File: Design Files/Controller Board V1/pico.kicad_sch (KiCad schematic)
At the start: 0 parts

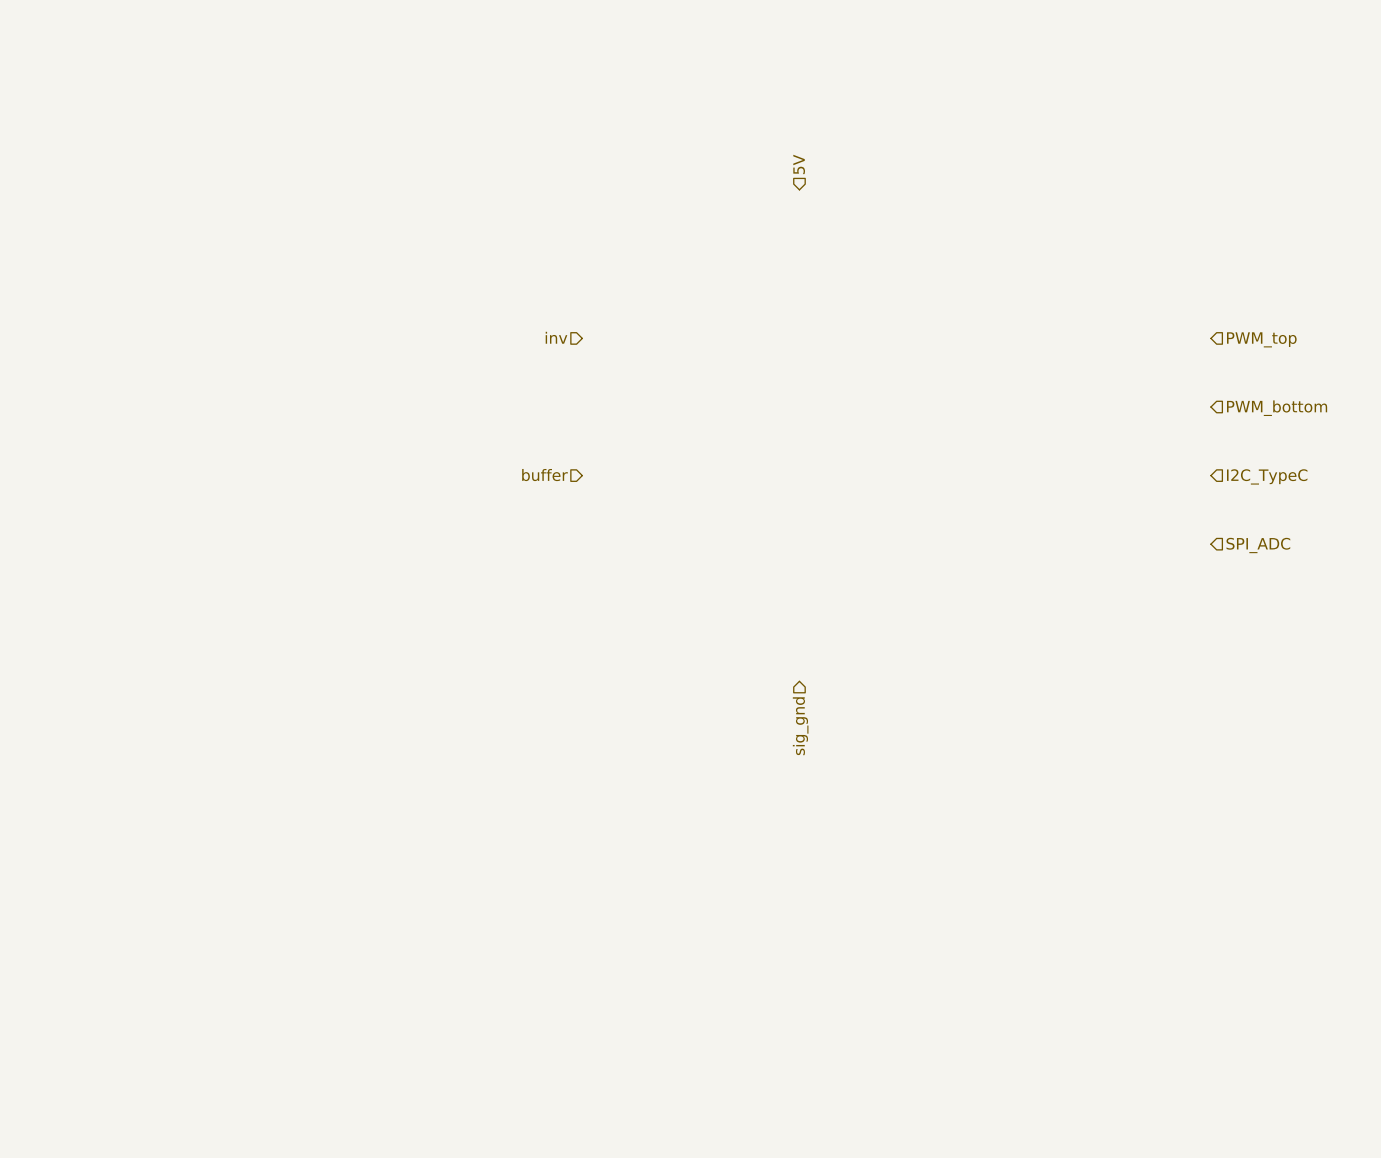
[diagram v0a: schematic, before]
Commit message: Pico Schematic Started
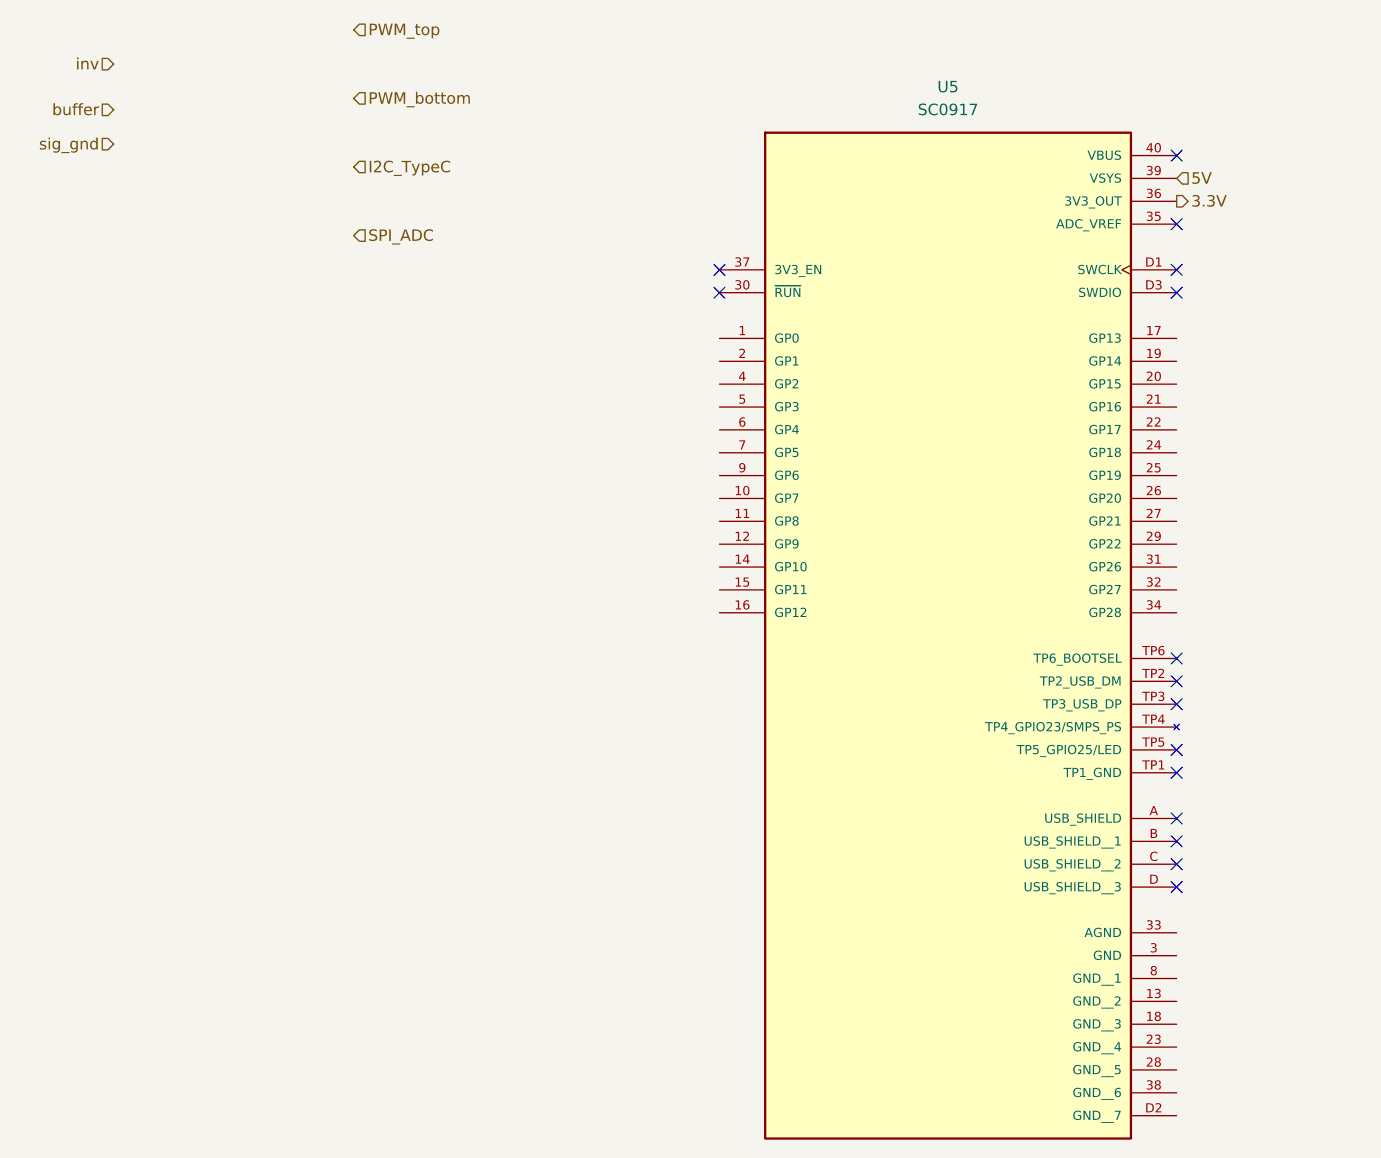
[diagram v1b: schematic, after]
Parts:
- added U5: SC0917, SC0917:MODULE_SC0917, symbol PassiveBankV1:SC0917
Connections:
- net 5V: now also U5.39 (VSYS)
- new net 3.3V: U5.36 (3V3_OUT)
- no-connect marks 0 -> 15

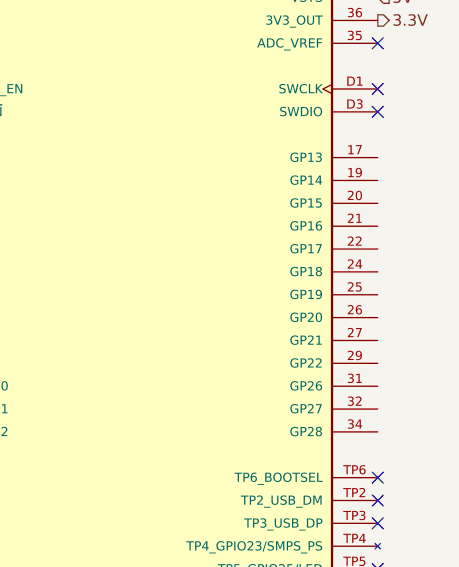
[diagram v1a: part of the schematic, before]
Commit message: I2C channels for pico and current sensors
gaming B)
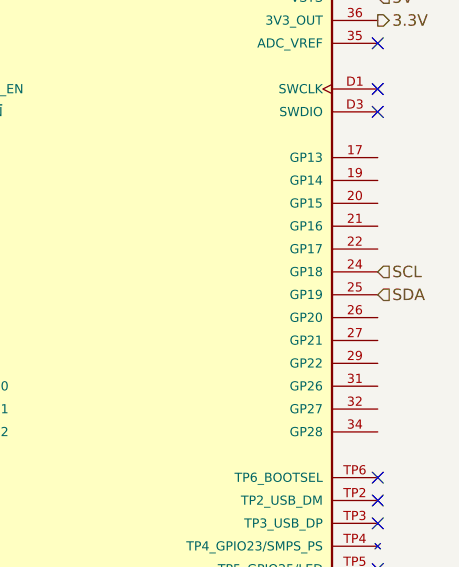
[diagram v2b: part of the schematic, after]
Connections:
- net SCL: now reaches U5.24 (GP18)
- net SDA: now reaches U5.25 (GP19)
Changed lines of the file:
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@@
 		(shape input)
 		(at 67.31 41.91 0)
+		(fields_autoplaced yes)
 		(effects
 			(font
@@
 		(shape input)
 		(at 40.64 46.99 180)
+		(fields_autoplaced yes)
 		(effects
 			(font
@@
 		(shape input)
 		(at 40.64 38.1 180)
+		(fields_autoplaced yes)
 		(effects
 			(font
@@
 		(shape output)
 		(at 158.75 53.34 0)
+		(fields_autoplaced yes)
 		(effects
 			(font
@@
 		(shape input)
 		(at 67.31 49.53 0)
+		(fields_autoplaced yes)
+		(effects
+			(font
+				(size 1.27 1.27)
+			)
+			(justify left)
+		)
+	)
+	(hierarchical_label "SCL"
+		(shape input)
+		(at 158.75 81.28 0)
+		(fields_autoplaced yes)
 		(effects
 			(font
@@
 		(shape input)
 		(at 67.31 57.15 0)
+		(fields_autoplaced yes)
+		(effects
+			(font
+				(size 1.27 1.27)
+			)
+			(justify left)
+		)
+	)
+	(hierarchical_label "SDA"
+		(shape input)
+		(at 158.75 83.82 0)
+		(fields_autoplaced yes)
 		(effects
 			(font
@@
 		(shape input)
 		(at 158.75 50.8 0)
+		(fields_autoplaced yes)
 		(effects
 			(font
@@
 		(shape input)
 		(at 67.31 34.29 0)
+		(fields_autoplaced yes)
 		(effects
 			(font
@@
 		(shape input)
 		(at 40.64 43.18 180)
+		(fields_autoplaced yes)
 		(effects
 			(font

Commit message: Assigning footprints and ading to schematic
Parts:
- U5: footprint SC0917:MODULE_SC0917 -> Module:RaspberryPi_Pico_Common_THT
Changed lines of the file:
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@@
 		(shape input)
 		(at 67.31 41.91 0)
-		(fields_autoplaced yes)
 		(effects
 			(font
@@
 		(shape input)
 		(at 40.64 46.99 180)
-		(fields_autoplaced yes)
 		(effects
 			(font
@@
 		(shape input)
 		(at 40.64 38.1 180)
-		(fields_autoplaced yes)
 		(effects
 			(font
@@
 		(shape output)
 		(at 158.75 53.34 0)
-		(fields_autoplaced yes)
 		(effects
 			(font
@@
 		(shape input)
 		(at 67.31 49.53 0)
-		(fields_autoplaced yes)
 		(effects
 			(font
@@
 		(shape input)
 		(at 158.75 81.28 0)
-		(fields_autoplaced yes)
 		(effects
 			(font
@@
 		(shape input)
 		(at 67.31 57.15 0)
-		(fields_autoplaced yes)
 		(effects
 			(font
@@
 		(shape input)
 		(at 158.75 83.82 0)
-		(fields_autoplaced yes)
 		(effects
 			(font
@@
 		(shape input)
 		(at 158.75 50.8 0)
-		(fields_autoplaced yes)
 		(effects
 			(font
@@
 		(shape input)
 		(at 67.31 34.29 0)
-		(fields_autoplaced yes)
 		(effects
 			(font
@@
 		(shape input)
 		(at 40.64 43.18 180)
-		(fields_autoplaced yes)
 		(effects
 			(font
@@
 			)
 		)
-		(property "Footprint" "SC0917:MODULE_SC0917"
+		(property "Footprint" "Module:RaspberryPi_Pico_Common_THT"
 			(at 133.35 88.9 0)
 			(effects

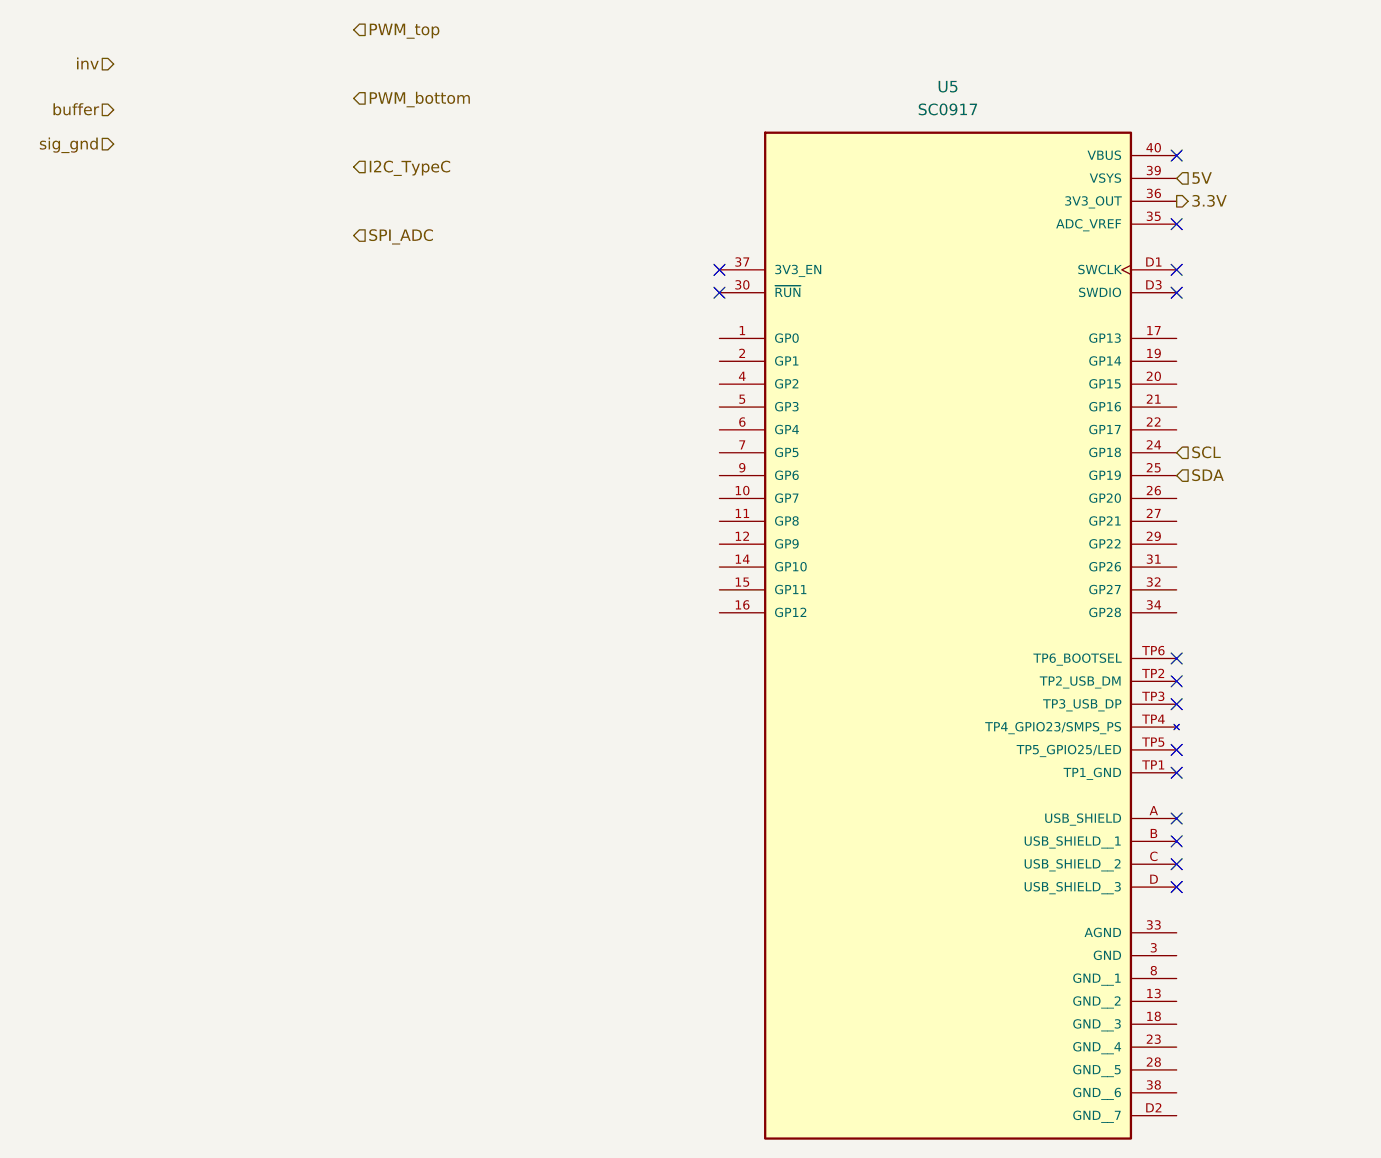
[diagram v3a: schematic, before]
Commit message: Updated pins on PICO schematic
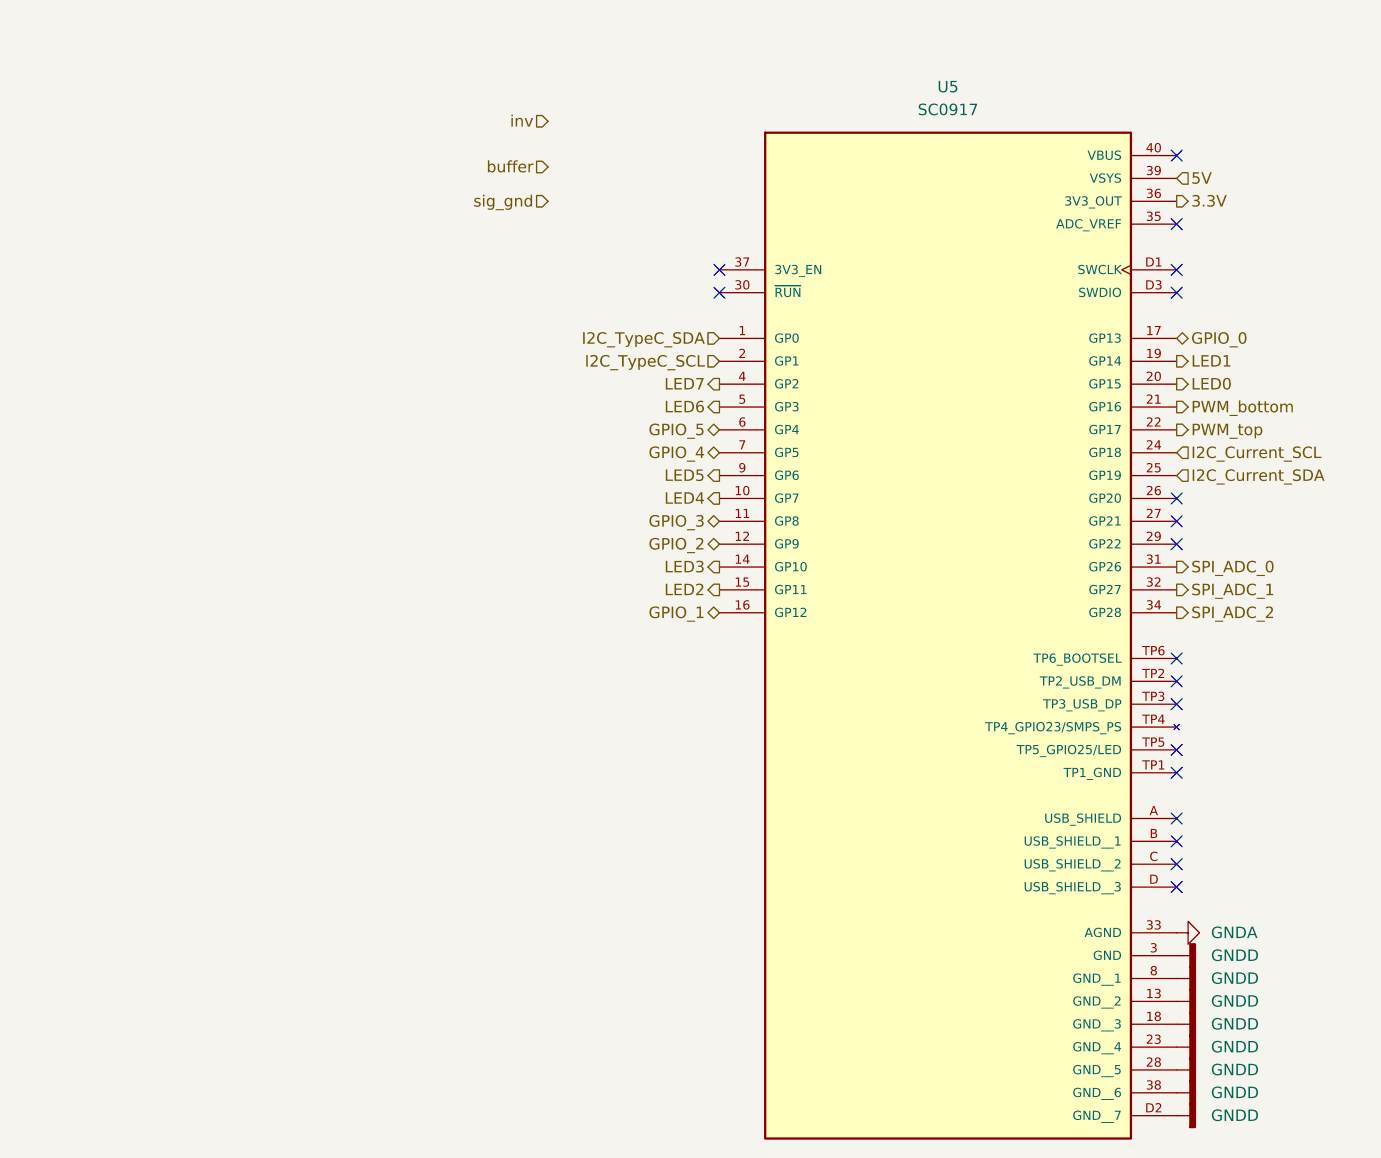
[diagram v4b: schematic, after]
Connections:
- net PWM_bottom: now also U5.21 (GP16)
- net PWM_top: now also U5.22 (GP17)
- net I2C_TypeC_SDA: now reaches U5.1 (GP0)
- net LED4: now reaches U5.10 (GP7)
- net GPIO_3: now reaches U5.11 (GP8)
- net GPIO_2: now reaches U5.12 (GP9)
- net GNDD: now reaches U5.13 (GND__2)
- net GNDD: now also U5.18 (GND__3), U5.23 (GND__4), U5.28 (GND__5), U5.3 (GND), U5.38 (GND__6), U5.8 (GND__1), U5.D2 (GND__7)
- net LED3: now reaches U5.14 (GP10)
- net LED2: now reaches U5.15 (GP11)
- net GPIO_1: now reaches U5.16 (GP12)
- net GPIO_0: now reaches U5.17 (GP13)
- net LED1: now reaches U5.19 (GP14)
- net I2C_TypeC_SCL: now reaches U5.2 (GP1)
- net LED0: now reaches U5.20 (GP15)
- net SPI_ADC_0: now reaches U5.31 (GP26)
- net SPI_ADC_1: now reaches U5.32 (GP27)
- net GNDA: now reaches U5.33 (AGND)
- net SPI_ADC_2: now reaches U5.34 (GP28)
- net LED7: now reaches U5.4 (GP2)
- net LED6: now reaches U5.5 (GP3)
- net GPIO_5: now reaches U5.6 (GP4)
- net GPIO_4: now reaches U5.7 (GP5)
- net LED5: now reaches U5.9 (GP6)
- net SCL renamed I2C_Current_SCL
- net SDA renamed I2C_Current_SDA
- no-connect marks 15 -> 18

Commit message: Major Schematic Progress
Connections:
- net SPI_ADC_0 renamed ADC_0
- net SPI_ADC_1 renamed ADC_1
- net SPI_ADC_2 renamed ADC_2
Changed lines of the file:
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@@
 		(shape bidirectional)
 		(at 107.95 81.28 180)
+		(fields_autoplaced yes)
 		(effects
 			(font
@@
 		(shape bidirectional)
 		(at 107.95 91.44 180)
-		(effects
-			(font
-				(size 1.27 1.27)
-			)
-			(justify right)
-		)
-	)
-	(hierarchical_label "SPI_ADC_1"
+		(fields_autoplaced yes)
+		(effects
+			(font
+				(size 1.27 1.27)
+			)
+			(justify right)
+		)
+	)
+	(hierarchical_label "ADC_1"
 		(shape output)
 		(at 158.75 96.52 0)
+		(fields_autoplaced yes)
 		(effects
 			(font
@@
 		(shape bidirectional)
 		(at 107.95 78.74 180)
+		(fields_autoplaced yes)
 		(effects
 			(font
@@
 		(shape output)
 		(at 158.75 76.2 0)
+		(fields_autoplaced yes)
 		(effects
 			(font
@@
 		(shape input)
 		(at 88.9 53.34 180)
+		(fields_autoplaced yes)
 		(effects
 			(font
@@
 		(shape input)
 		(at 88.9 44.45 180)
+		(fields_autoplaced yes)
 		(effects
 			(font
@@
 		(shape output)
 		(at 107.95 83.82 180)
+		(fields_autoplaced yes)
 		(effects
 			(font
@@
 		(shape output)
 		(at 107.95 73.66 180)
+		(fields_autoplaced yes)
 		(effects
 			(font
@@
 		(shape output)
 		(at 107.95 93.98 180)
+		(fields_autoplaced yes)
 		(effects
 			(font
@@
 		(shape output)
 		(at 158.75 73.66 0)
+		(fields_autoplaced yes)
 		(effects
 			(font
@@
 		(shape output)
 		(at 158.75 53.34 0)
+		(fields_autoplaced yes)
 		(effects
 			(font
@@
 		(shape input)
 		(at 107.95 68.58 180)
+		(fields_autoplaced yes)
 		(effects
 			(font
@@
 		(shape bidirectional)
 		(at 158.75 68.58 0)
+		(fields_autoplaced yes)
 		(effects
 			(font
@@
 	)
 	(hierarchical_label "I2C_Current_SCL"
-		(shape input)
+		(shape bidirectional)
 		(at 158.75 81.28 0)
-		(effects
-			(font
-				(size 1.27 1.27)
-			)
-			(justify left)
-		)
-	)
-	(hierarchical_label "SPI_ADC_0"
+		(fields_autoplaced yes)
+		(effects
+			(font
+				(size 1.27 1.27)
+			)
+			(justify left)
+		)
+	)
+	(hierarchical_label "ADC_0"
 		(shape output)
 		(at 158.75 93.98 0)
+		(fields_autoplaced yes)
 		(effects
 			(font
@@
 		(shape bidirectional)
 		(at 107.95 88.9 180)
+		(fields_autoplaced yes)
 		(effects
 			(font
@@
 		(shape input)
 		(at 107.95 71.12 180)
-		(effects
-			(font
-				(size 1.27 1.27)
-			)
-			(justify right)
-		)
-	)
-	(hierarchical_label "SPI_ADC_2"
+		(fields_autoplaced yes)
+		(effects
+			(font
+				(size 1.27 1.27)
+			)
+			(justify right)
+		)
+	)
+	(hierarchical_label "ADC_2"
 		(shape output)
 		(at 158.75 99.06 0)
+		(fields_autoplaced yes)
 		(effects
 			(font
@@
 		(shape output)
 		(at 107.95 86.36 180)
+		(fields_autoplaced yes)
 		(effects
 			(font
@@
 	)
 	(hierarchical_label "I2C_Current_SDA"
-		(shape input)
+		(shape bidirectional)
 		(at 158.75 83.82 0)
+		(fields_autoplaced yes)
 		(effects
 			(font
@@
 		(shape input)
 		(at 158.75 50.8 0)
+		(fields_autoplaced yes)
 		(effects
 			(font
@@
 		(shape bidirectional)
 		(at 107.95 99.06 180)
+		(fields_autoplaced yes)
 		(effects
 			(font
@@
 		(shape output)
 		(at 107.95 76.2 180)
+		(fields_autoplaced yes)
 		(effects
 			(font
@@
 		(shape output)
 		(at 158.75 78.74 0)
+		(fields_autoplaced yes)
 		(effects
 			(font
@@
 		(shape input)
 		(at 88.9 49.53 180)
+		(fields_autoplaced yes)
 		(effects
 			(font
@@
 		(shape output)
 		(at 158.75 71.12 0)
+		(fields_autoplaced yes)
 		(effects
 			(font
@@
 		(shape output)
 		(at 107.95 96.52 180)
-		(effects
-			(font
+		(fields_autoplaced yes)
+		(effects
+			(font
